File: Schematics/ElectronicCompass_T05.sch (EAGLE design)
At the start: 61 parts, among them Q1 FDN360P, Q2 FDN360P, Q3 FDN360P, Q4 FDN360P, U1 ATMEGA32U4, X1 USBSMD, Y1 16MHz

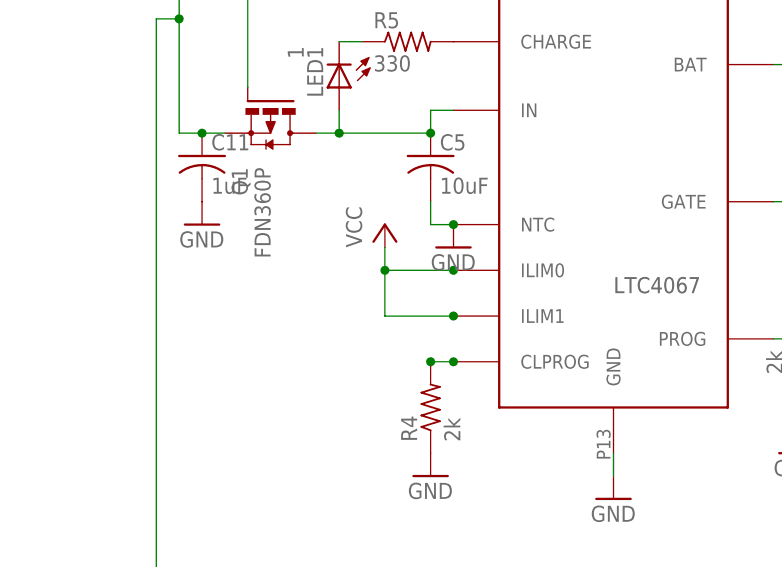
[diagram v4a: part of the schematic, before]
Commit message: Grounded current limiting programming pins on PMIC
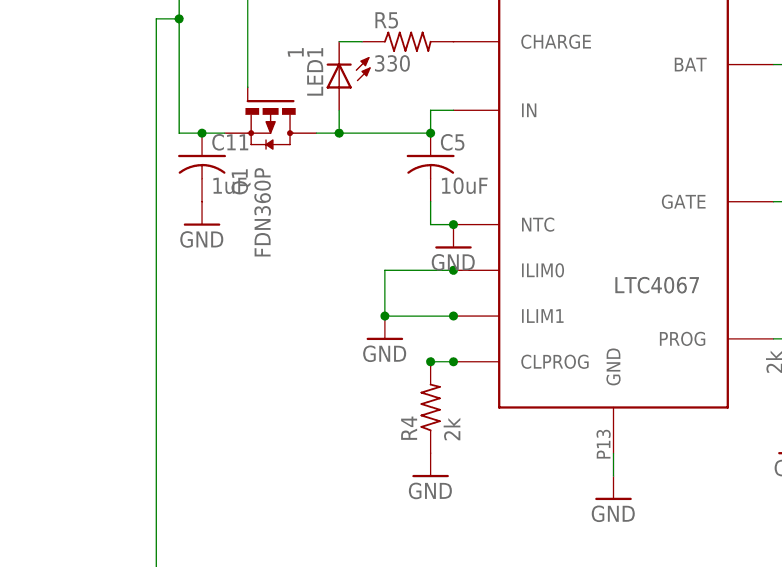
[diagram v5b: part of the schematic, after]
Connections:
- net GND: now also U$1.ILIM0, U$1.ILIM1
- net VCC: no longer U$1.ILIM0, U$1.ILIM1
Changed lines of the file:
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@@
 <part name="GND15" library="supply1" deviceset="GND" device=""/>
 <part name="GND16" library="supply1" deviceset="GND" device=""/>
-<part name="P+5" library="supply1" deviceset="VCC" device=""/>
 <part name="LED1" library="led" deviceset="LED" device="CHIPLED_0805" value="1"/>
 <part name="Q2" library="transistor-power" deviceset="FDN360P" device=""/>
@@
 <part name="C6" library="SparkFun" deviceset="CAP" device="0402-CAP" value="18pF"/>
 <part name="GND3" library="SparkFun" deviceset="GND" device=""/>
+<part name="GND6" library="supply1" deviceset="GND" device=""/>
 </parts>
 <sheets>
@@
 <instance part="GND15" gate="1" x="71.12" y="10.16"/>
 <instance part="GND16" gate="1" x="30.48" y="7.62"/>
-<instance part="P+5" gate="VCC" x="25.4" y="35.56"/>
 <instance part="LED1" gate="G$1" x="20.32" y="50.8" rot="R180"/>
 <instance part="Q2" gate="G$1" x="78.74" y="50.8"/>
@@
 </instance>
 <instance part="GND3" gate="1" x="116.84" y="-30.48"/>
+<instance part="GND6" gate="1" x="25.4" y="22.86"/>
 </instances>
 <busses>
@@
 <wire x1="50.8" y1="7.62" x2="50.8" y2="10.16" width="0.1524" layer="91"/>
 </segment>
+<segment>
+<wire x1="33.02" y1="25.4" x2="25.4" y2="25.4" width="0.1524" layer="91"/>
+<wire x1="25.4" y1="25.4" x2="25.4" y2="30.48" width="0.1524" layer="91"/>
+<wire x1="33.02" y1="30.48" x2="25.4" y2="30.48" width="0.1524" layer="91"/>
+<pinref part="U$1" gate="G$1" pin="ILIM1"/>
+<junction x="33.02" y="25.4"/>
+<pinref part="U$1" gate="G$1" pin="ILIM0"/>
+<junction x="33.02" y="30.48"/>
+<pinref part="GND6" gate="1" pin="GND"/>
+<junction x="25.4" y="25.4"/>
+</segment>
 </net>
 <net name="VCC" class="0">
@@
 </segment>
 <segment>
-<wire x1="33.02" y1="25.4" x2="25.4" y2="25.4" width="0.1524" layer="91"/>
-<pinref part="P+5" gate="VCC" pin="VCC"/>
-<wire x1="25.4" y1="25.4" x2="25.4" y2="30.48" width="0.1524" layer="91"/>
-<wire x1="25.4" y1="30.48" x2="25.4" y2="33.02" width="0.1524" layer="91"/>
-<wire x1="33.02" y1="30.48" x2="25.4" y2="30.48" width="0.1524" layer="91"/>
-<junction x="25.4" y="30.48"/>
-<pinref part="U$1" gate="G$1" pin="ILIM1"/>
-<junction x="33.02" y="25.4"/>
-<pinref part="U$1" gate="G$1" pin="ILIM0"/>
-<junction x="33.02" y="30.48"/>
-</segment>
-<segment>

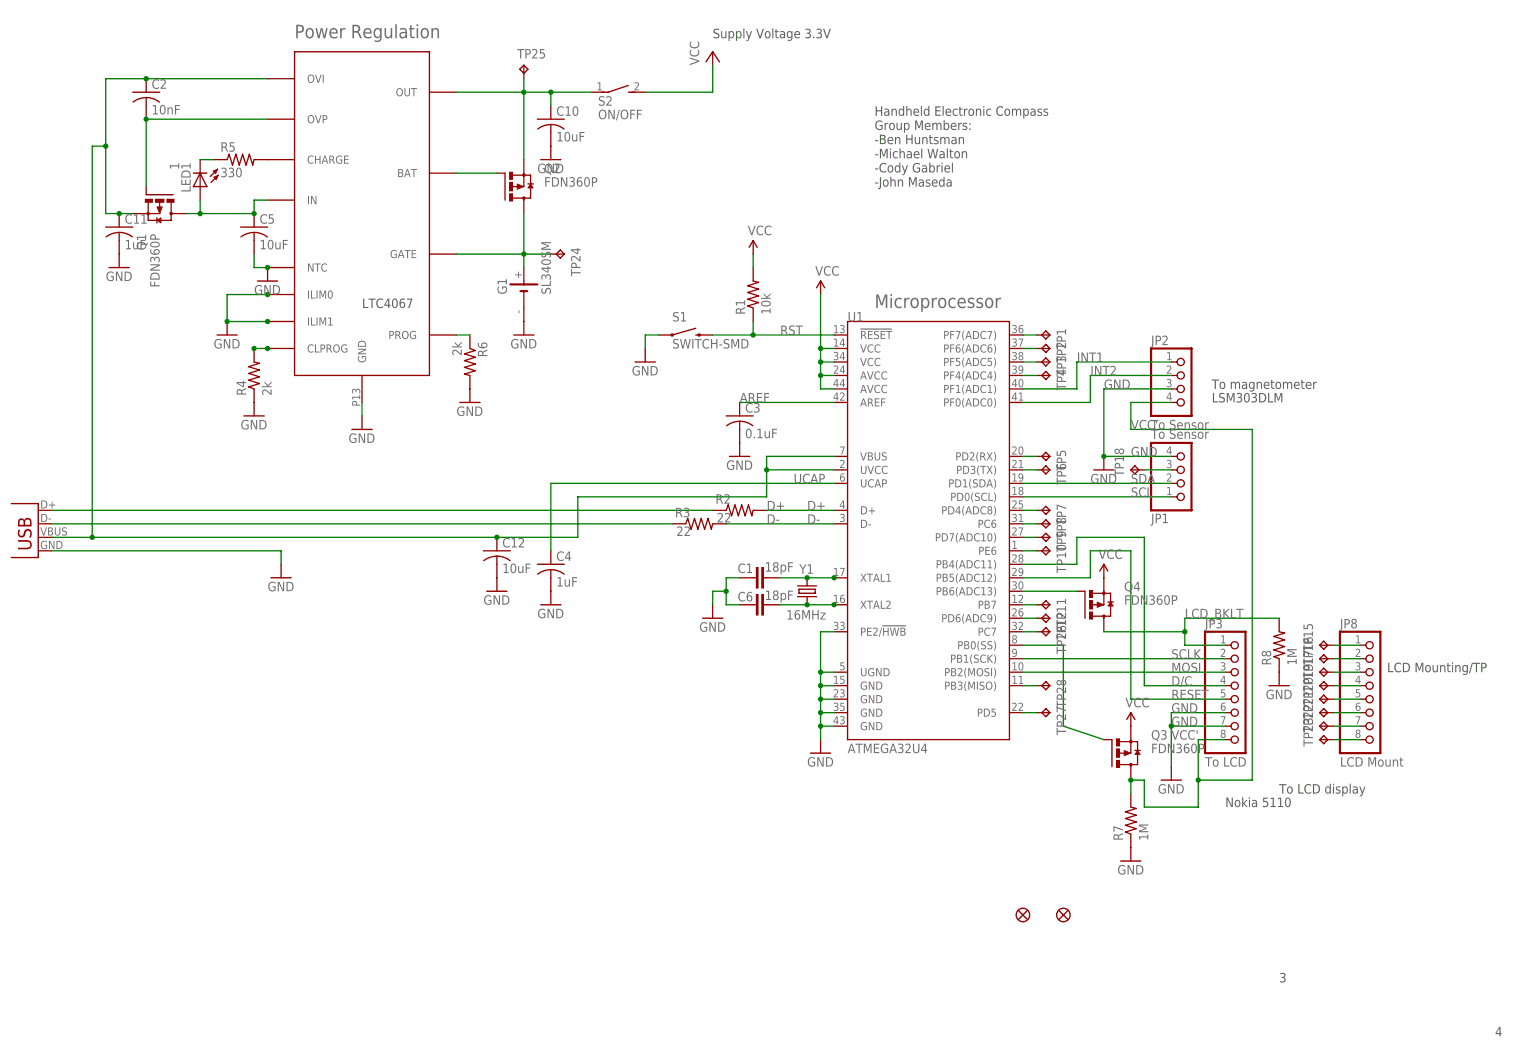
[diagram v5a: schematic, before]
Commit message: Made some changes to the schematic recommended by Andrew. It is not finished yet but there are some major changes that need to be done before we turn this thing in.
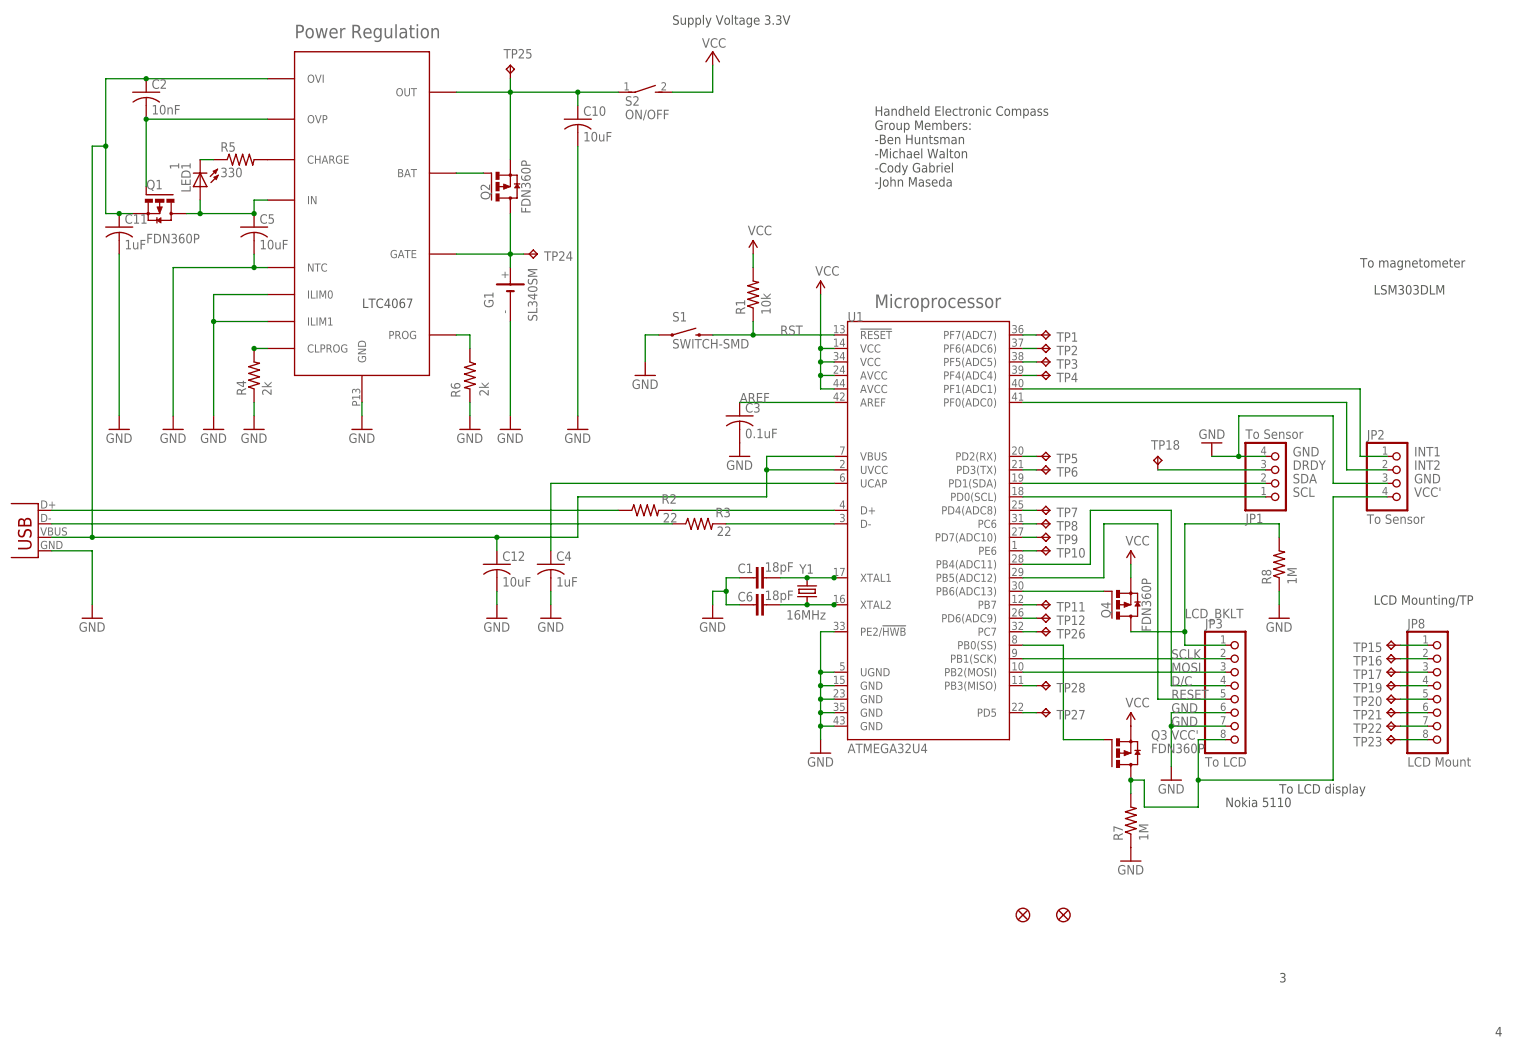
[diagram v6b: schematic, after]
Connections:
- net D+ renamed N$34
- net N$11 renamed VBUS
- net N$34 renamed DRDY
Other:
- moved on the sheet: C10, C12, G1, JP1, JP2, JP8, Q2, Q4, R2, R6, R8, S2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

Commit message: Made some more updates to the schematic according to what Andrew suggested. Still need to put in the new batter header and then fix the board layout.
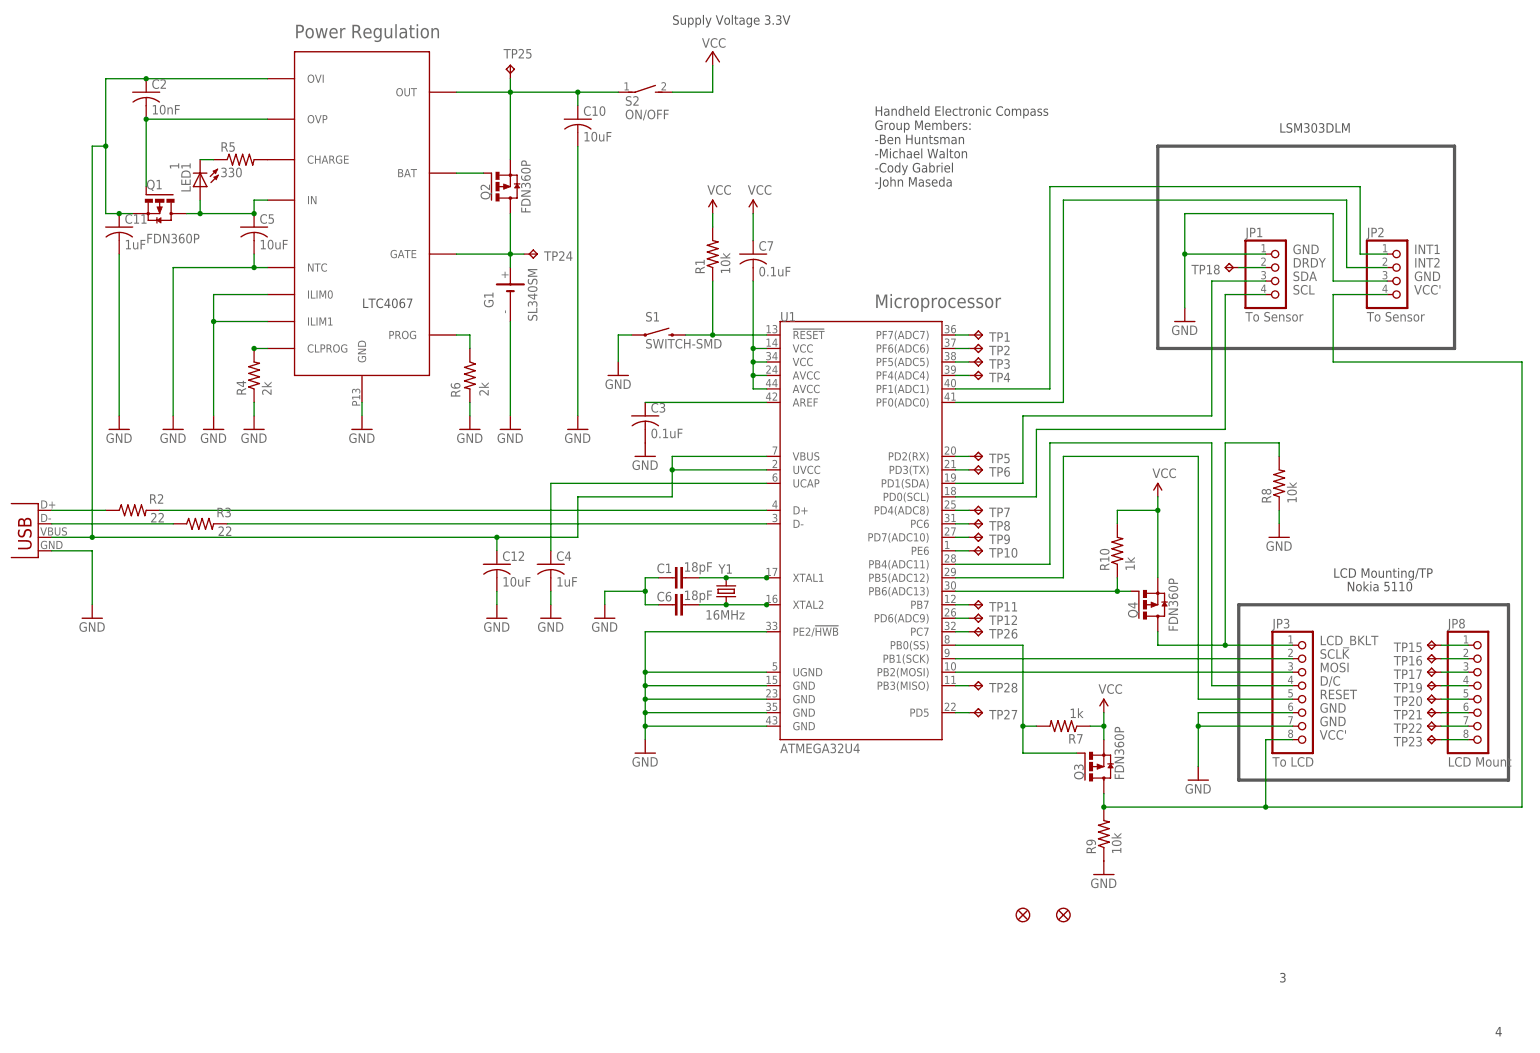
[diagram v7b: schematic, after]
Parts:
- added C7: 0.1uF, rcl:C-USC0805
- added R10: 1k, resistor:R-US_M0805
- added R9: 10k, resistor:R-US_M0805
- R7: value 1M -> 1k; device rcl:R-US_M0805 -> resistor:R-US_M0805
- R8: value 1M -> 10k
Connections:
- net AREF renamed N$38
- new net N$11: C7.2, U1.AVCC@24, U1.AVCC@44, U1.VCC@14, U1.VCC@34
- net DRDY: now also JP1.2; no longer JP1.3
- net GND: now also JP1.1, R9.1; no longer JP1.4, R7.1
- net N$26: now also R10.1
- net N$37: now also R7.2
- net SCL: now also JP1.4; no longer JP1.1
- net SDA: now also JP1.3; no longer JP1.2
- net VCC: now also C7.1, R10.2, R7.1; no longer U1.AVCC@24, U1.AVCC@44, U1.VCC@14, U1.VCC@34
- net VCC': now also R9.2; no longer R7.2
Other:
- note removed: "To LCD display"
- note removed: "To magnetometer"
- moved on the sheet: C1, C3, C6, JP1, JP2, JP3, JP8, Q3, Q4, R1, R2, R3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

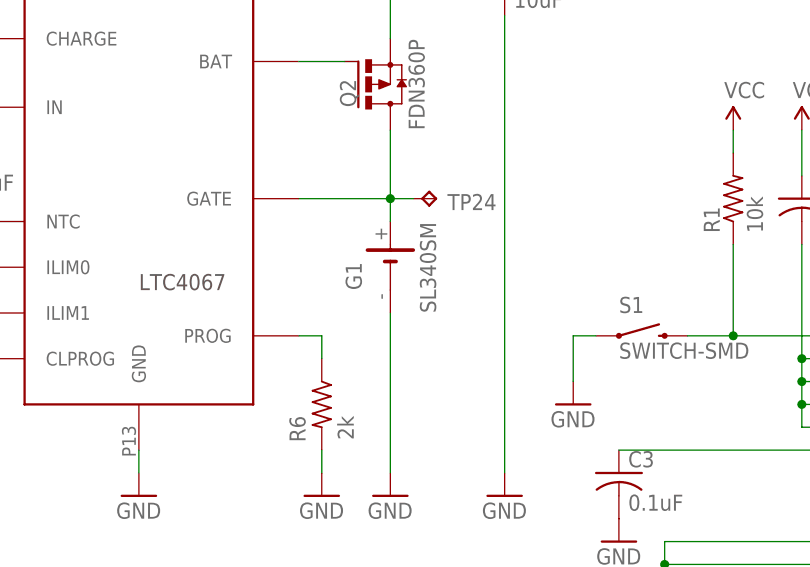
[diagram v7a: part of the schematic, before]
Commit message: Made some updates to the schem and board.  Still a lot of issues with the board layout that need to be worked out.
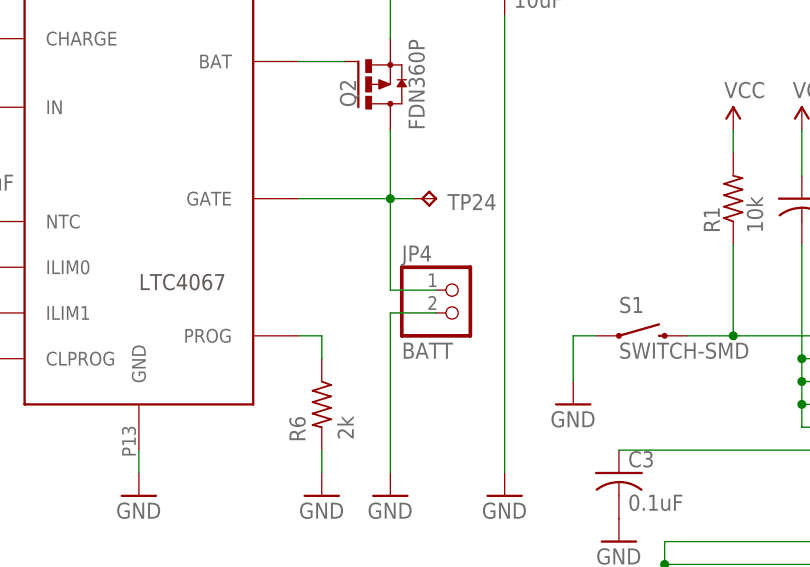
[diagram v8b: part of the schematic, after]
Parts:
- removed G1: SL340SM, battery:SL340SM
- added JP4: BATT, pinhead:PINHD-1X2
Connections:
- net GND: now also JP4.2; no longer G1.-
- net N$5: now also JP4.1; no longer G1.+
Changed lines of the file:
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@@
 <part name="GND17" library="supply1" deviceset="GND" device=""/>
 <part name="GND18" library="supply1" deviceset="GND" device=""/>
-<part name="G1" library="battery" deviceset="SL340SM" device=""/>
 <part name="GND19" library="supply1" deviceset="GND" device=""/>
 <part name="P+3" library="supply1" deviceset="VCC" device=""/>
@@
 <part name="R9" library="resistor" deviceset="R-US_" device="M0805" value="10k"/>
 <part name="R10" library="resistor" deviceset="R-US_" device="M0805" value="1k"/>
+<part name="JP4" library="pinhead" deviceset="PINHD-1X2" device="" value="BATT"/>
 </parts>
 <sheets>
@@
 <instance part="GND17" gate="1" x="76.2" y="-30.48"/>
 <instance part="GND18" gate="1" x="15.24" y="5.08"/>
-<instance part="G1" gate="G$1" x="78.74" y="30.48" smashed="yes" rot="R90">
-<attribute name="NAME" x="75.565" y="27.94" size="1.778" layer="95" rot="R90"/>
-<attribute name="VALUE" x="83.82" y="25.4" size="1.778" layer="96" rot="R90"/>
-</instance>
 <instance part="GND19" gate="1" x="78.74" y="5.08"/>
 <instance part="P+3" gate="VCC" x="116.84" y="76.2" smashed="yes">
@@
 <attribute name="VALUE" x="196.342" y="-21.59" size="1.778" layer="96" rot="R90"/>
 </instance>
+<instance part="JP4" gate="G$1" x="86.36" y="25.4"/>
 </instances>
 <busses>
@@
 </segment>
 <segment>
-<pinref part="G1" gate="G$1" pin="-"/>
-<pinref part="GND19" gate="1" pin="GND"/>
-<wire x1="78.74" y1="7.62" x2="78.74" y2="25.4" width="0.1524" layer="91"/>
-</segment>
-<segment>
 <pinref part="C4" gate="G$1" pin="2"/>
 <pinref part="GND12" gate="1" pin="GND"/>
@@
 <wire x1="220.98" y1="38.1" x2="205.74" y2="38.1" width="0.1524" layer="91"/>
 <junction x="205.74" y="38.1"/>
+</segment>
+<segment>
+<pinref part="GND19" gate="1" pin="GND"/>
+<wire x1="78.74" y1="7.62" x2="78.74" y2="25.4" width="0.1524" layer="91"/>
+<pinref part="JP4" gate="G$1" pin="2"/>
+<wire x1="78.74" y1="25.4" x2="83.82" y2="25.4" width="0.1524" layer="91"/>
 </segment>
 </net>
@@
 <wire x1="68.58" y1="38.1" x2="78.74" y2="38.1" width="0.1524" layer="91"/>
 <pinref part="TP24" gate="G$1" pin="TP"/>
-<pinref part="G1" gate="G$1" pin="+"/>
 <wire x1="78.74" y1="38.1" x2="81.28" y2="38.1" width="0.1524" layer="91"/>
-<wire x1="78.74" y1="35.56" x2="78.74" y2="38.1" width="0.1524" layer="91"/>
 <pinref part="Q2" gate="G$1" pin="D"/>
 <wire x1="78.74" y1="38.1" x2="78.74" y2="45.72" width="0.1524" layer="91"/>
 <junction x="78.74" y="38.1"/>
 <pinref part="U$1" gate="G$1" pin="GATE"/>
-</segment>
-</net>
+<wire x1="78.74" y1="38.1" x2="78.74" y2="27.94" width="0.1524" layer="91"/>
+<pinref part="JP4" gate="G$1" pin="1"/>
+<wire x1="78.74" y1="27.94" x2="83.82" y2="27.94" width="0.1524" layer="91"/>
+</segment>
+</net>
